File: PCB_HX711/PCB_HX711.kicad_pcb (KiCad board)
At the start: 2 copper layers, 65 x 45 mm, 2 parts, among them J1 HX711, J2 Conn_01x04_Socket

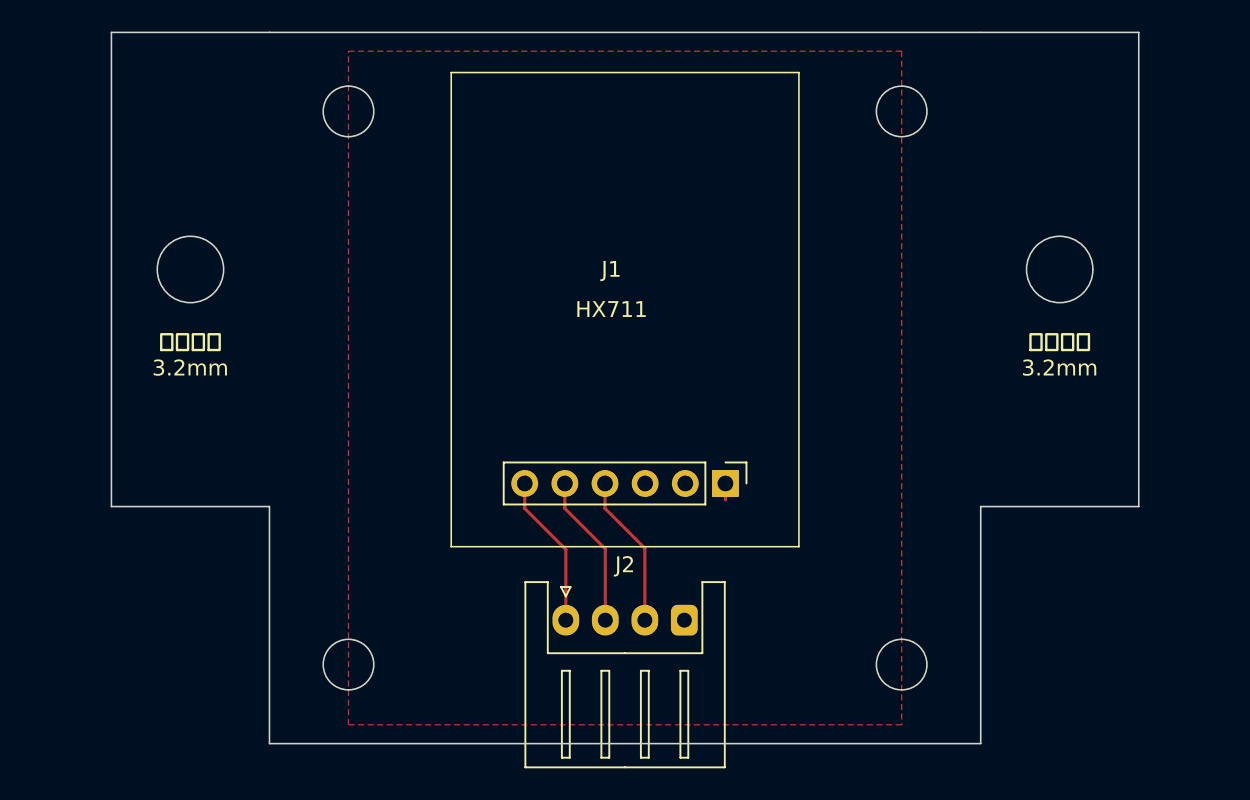
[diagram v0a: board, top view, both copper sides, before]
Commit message: Modify PCB_HX711
タッピングの位置を離した
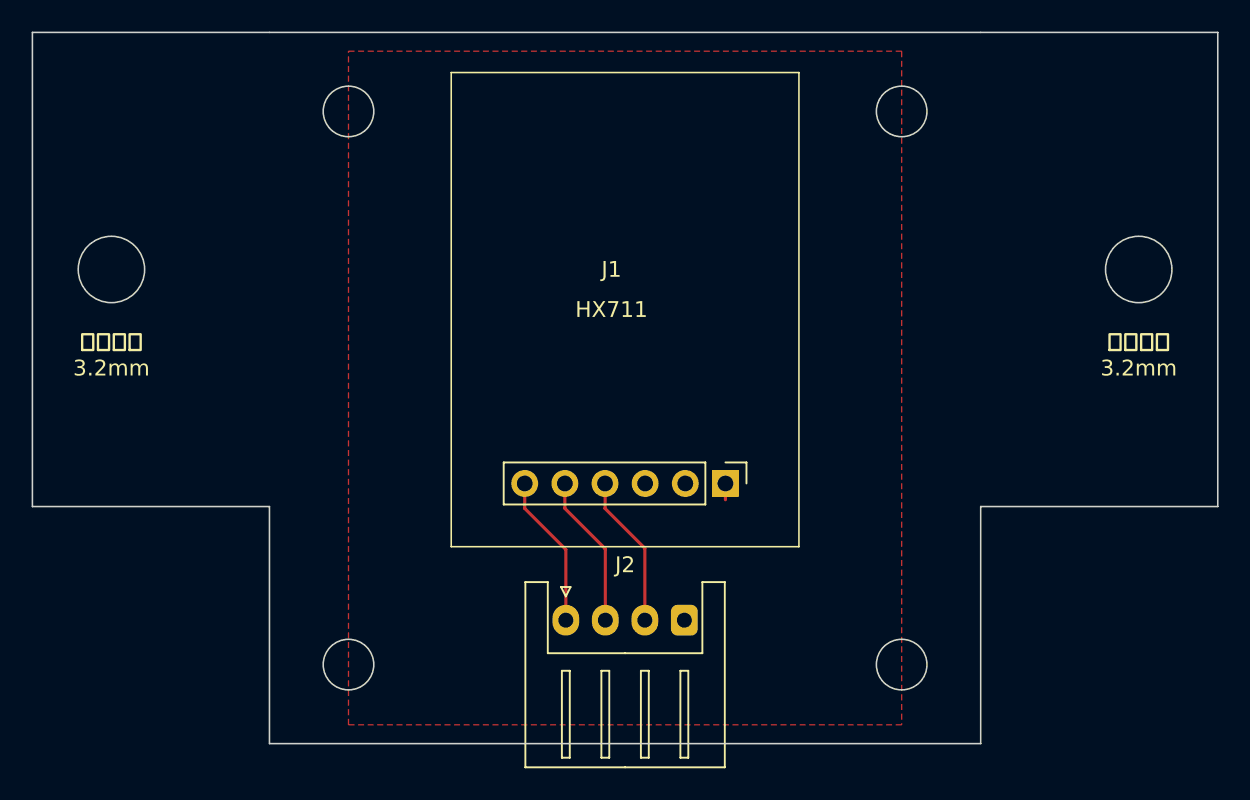
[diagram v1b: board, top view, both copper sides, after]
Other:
- board size 65 x 45 mm -> 75 x 45 mm
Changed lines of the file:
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@@
 	)
 	(gr_rect
-		(start 135.1 53.34)
-		(end 113.1 83.34)
+		(start 113.1 53.34)
+		(end 135.1 83.34)
 		(stroke
 			(width 0.1)
@@
 	)
 	(gr_circle
-		(center 96.6 65.8)
-		(end 98.7 65.8)
+		(center 91.6 65.8)
+		(end 93.7 65.8)
 		(stroke
 			(width 0.1)
@@
 	)
 	(gr_circle
-		(center 151.6 65.8)
-		(end 153.7 65.8)
-		(stroke
-			(width 0.1)
-			(type default)
-		)
-		(fill none)
-		(layer "Edge.Cuts")
-	)
-	(gr_line
-		(start 91.6 50.8)
+		(center 156.6 65.8)
+		(end 158.7 65.8)
+		(stroke
+			(width 0.1)
+			(type default)
+		)
+		(fill none)
+		(layer "Edge.Cuts")
+	)
+	(gr_line
+		(start 86.6 50.8)
 		(end 101.6 50.8)
 		(stroke
@@
 	)
 	(gr_line
-		(start 156.6 80.8)
+		(start 161.6 80.8)
 		(end 146.6 80.8)
 		(stroke
@@
 	)
 	(gr_line
-		(start 156.6 50.8)
-		(end 156.6 80.8)
+		(start 161.6 50.8)
+		(end 161.6 80.8)
 		(stroke
 			(width 0.1)
@@
 	(gr_line
 		(start 101.6 80.8)
-		(end 91.6 80.8)
+		(end 86.6 80.8)
 		(stroke
 			(width 0.1)
@@
 	(gr_line
 		(start 146.6 50.8)
-		(end 156.6 50.8)
+		(end 161.6 50.8)
 		(stroke
 			(width 0.1)
@@
 	)
 	(gr_line
-		(start 91.6 50.8)
-		(end 91.6 80.8)
+		(start 86.6 50.8)
+		(end 86.6 80.8)
 		(stroke
 			(width 0.1)
@@
 	(gr_line
 		(start 101.6 45.72)
-		(end 96.6 45.72)
+		(end 91.6 45.72)
 		(stroke
 			(width 0.1)
@@
 	(gr_line
 		(start 146.6 50.8)
-		(end 146.6 45.72)
+		(end 146.6 45.8)
 		(stroke
 			(width 0.1)
@@
 	)
 	(gr_line
-		(start 151.6 45.72)
-		(end 151.6 77.470101)
+		(start 156.6 45.8)
+		(end 156.6 65.8)
 		(stroke
 			(width 0.1)
@@
 	)
 	(gr_line
-		(start 151.6 45.72)
-		(end 146.6 45.72)
+		(start 156.6 45.8)
+		(end 146.6 45.8)
 		(stroke
 			(width 0.1)
@@
 	)
 	(gr_line
-		(start 96.6 45.72)
-		(end 96.6 77.470101)
-		(stroke
-			(width 0.1)
-			(type default)
-		)
-		(layer "User.2")
+		(start 91.6 45.72)
+		(end 91.6 77.470101)
+		(stroke
+			(width 0.1)
+			(type default)
+		)
+		(layer "User.2")
+	)
+	(gr_rect
+		(start 99.06 47.39)
+		(end 149.06 97.39)
+		(stroke
+			(width 0.1)
+			(type default)
+		)
+		(fill none)
+		(layer "User.4")
 	)
 	(gr_text "下穴の径\n3.2mm"
-		(at 151.6 69.85 0)
+		(at 156.6 69.85 0)
 		(layer "F.SilkS")
 		(effects
@@
 	)
 	(gr_text "下穴の径\n3.2mm"
-		(at 96.6 69.85 0)
+		(at 91.6 69.85 0)
 		(layer "F.SilkS")
 		(effects
